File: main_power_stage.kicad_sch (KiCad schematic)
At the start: 75 parts, among them SW1 CAS-120TA, U11 AP7366_SOT, U2 LV14540DDAR, U6 TPS65987DDHRSHR, U7 LV14540DDAR, U8 74CBTLV3257_VQFN, U9 W25Q80DV_SOIC-8

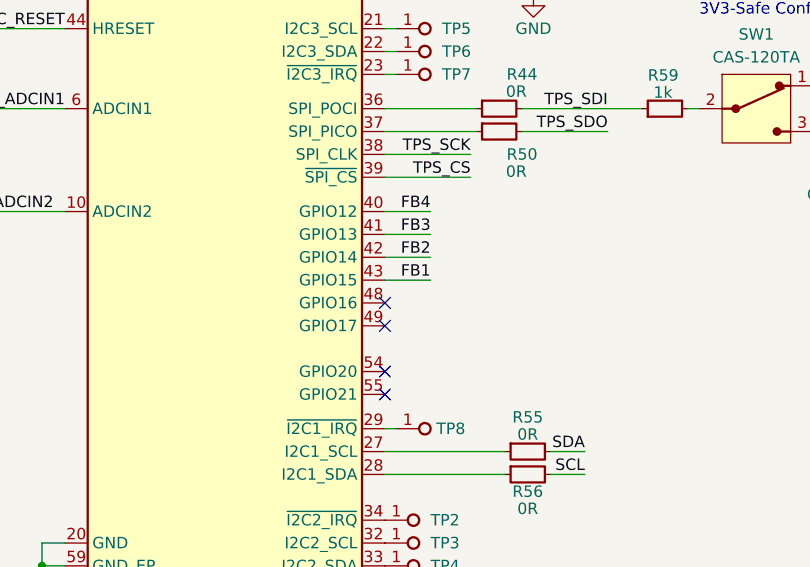
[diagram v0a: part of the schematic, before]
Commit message: [#63274] Change TPS65987 feedback for DCDC gpio pinout
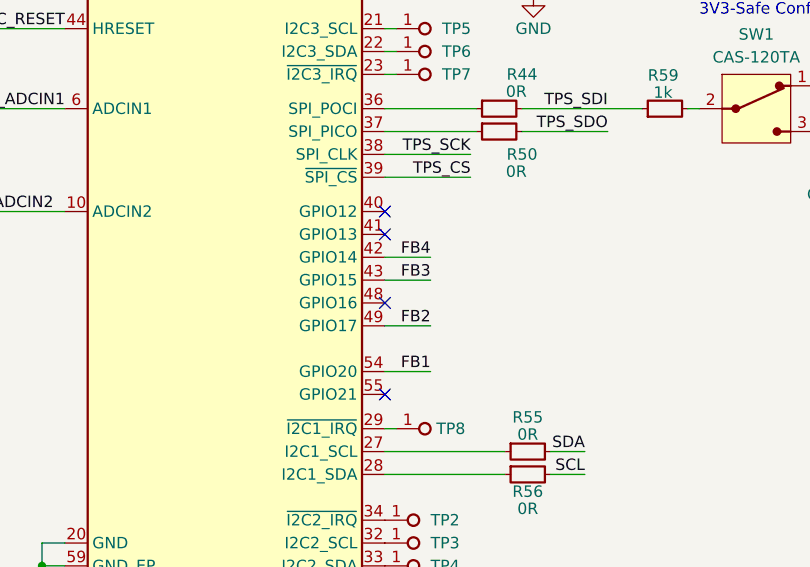
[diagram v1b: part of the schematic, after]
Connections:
- net FB1: now also U6.54 (GPIO20); no longer U6.43 (GPIO15)
- net FB2: now also U6.49 (GPIO17); no longer U6.42 (GPIO14)
- net FB3: now also U6.43 (GPIO15); no longer U6.41 (GPIO13)
- net FB4: now also U6.42 (GPIO14); no longer U6.40 (GPIO12)

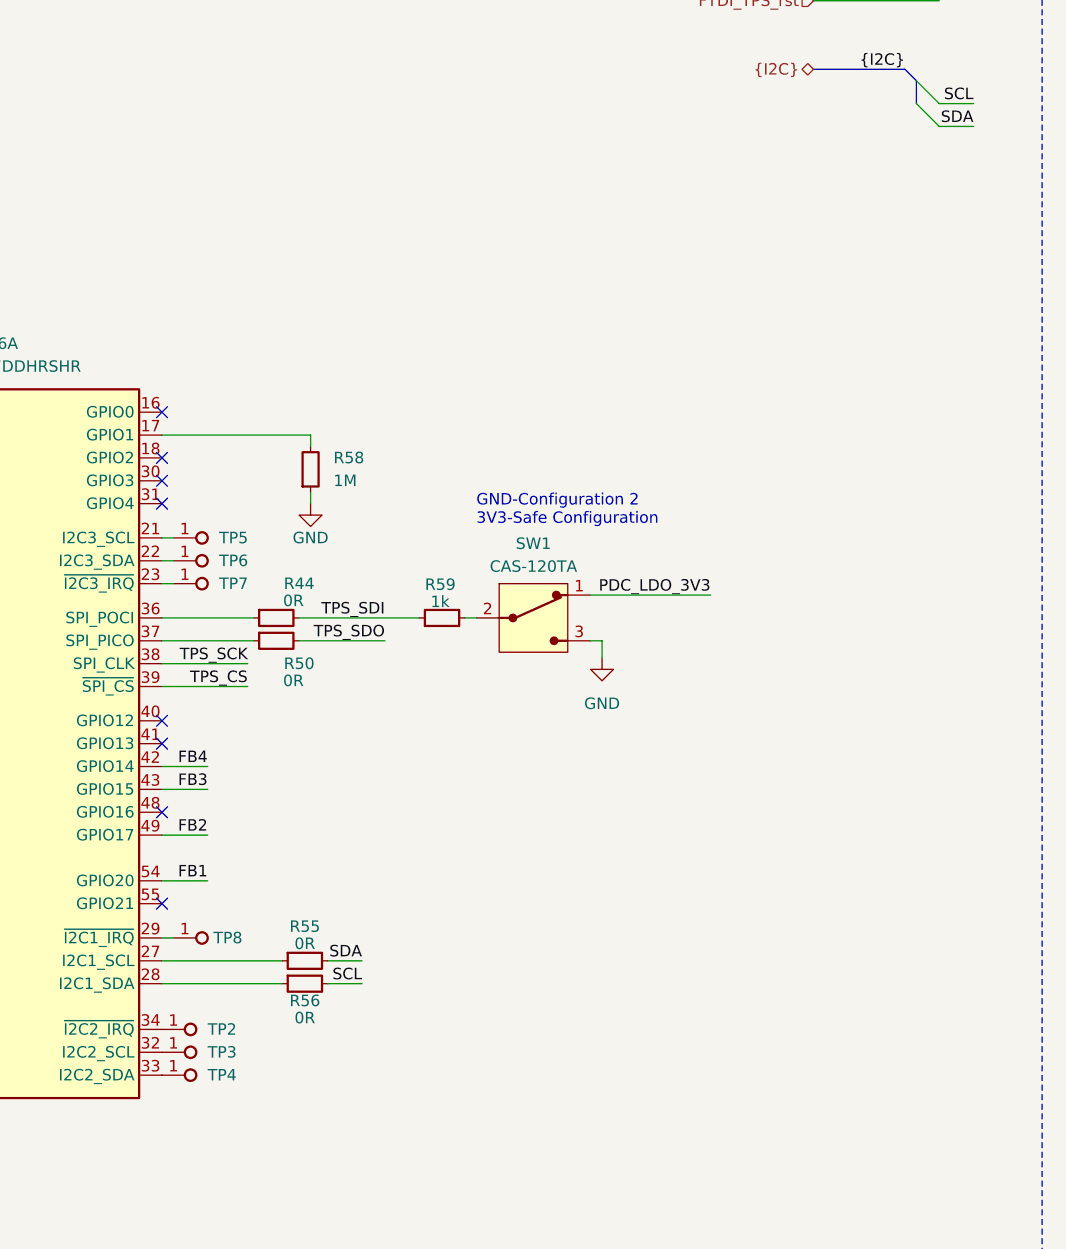
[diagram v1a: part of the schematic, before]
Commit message: [#63274] Add testpoints, improve silcscreen
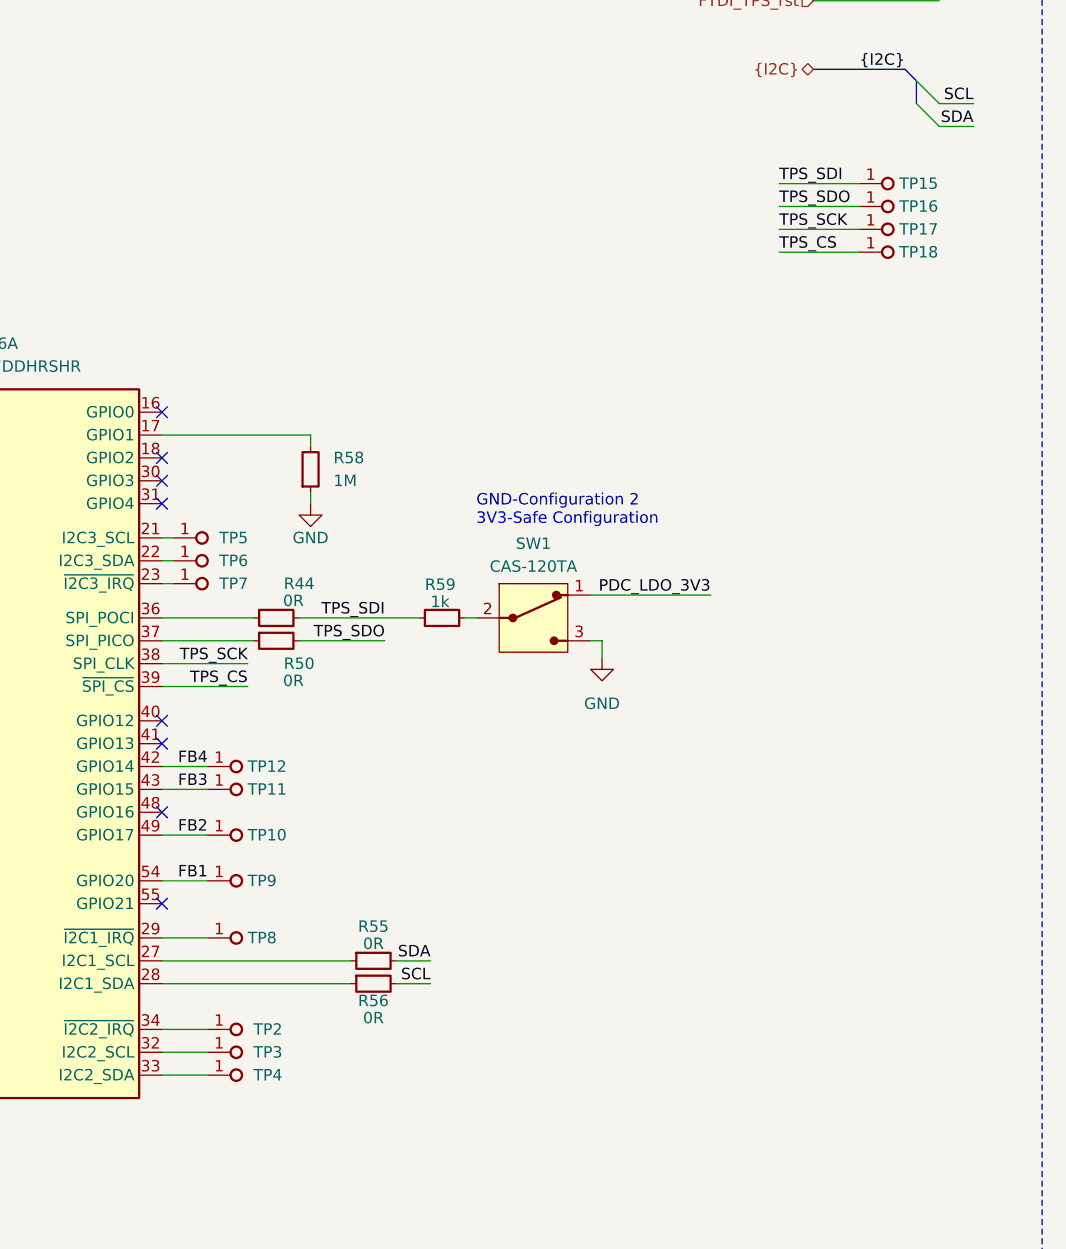
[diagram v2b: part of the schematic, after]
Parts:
- added TP10, TP11, TP12, TP15, TP16, TP17, TP18, TP9: TP_0.75mm_SMD, antmicro-footprints:TP_SMD_0.75mm, symbol antmicroTestPoints:TP_0.75mm_SMD
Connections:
- net FB1: now also TP9.1
- net FB2: now also TP10.1
- net FB3: now also TP11.1
- net FB4: now also TP12.1
- net TPS_CS: now also TP18.1
- net TPS_SCK: now also TP17.1
- net TPS_SDI: now also TP15.1
- net TPS_SDO: now also TP16.1
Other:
- moved on the sheet: R55, R56, TP2, TP3, TP4, TP8

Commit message: [#63274] Prepare for visualization and fabhouse
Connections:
- net FLASH_CS: now also TP18.1
- net FLASH_SCK: now also TP17.1
- net FLASH_SDI: now also TP16.1
- net FLASH_SDO: now also TP15.1
- net TPS_CS: no longer TP18.1
- net TPS_SCK: no longer TP17.1
- net TPS_SDI: no longer TP15.1
- net TPS_SDO: no longer TP16.1

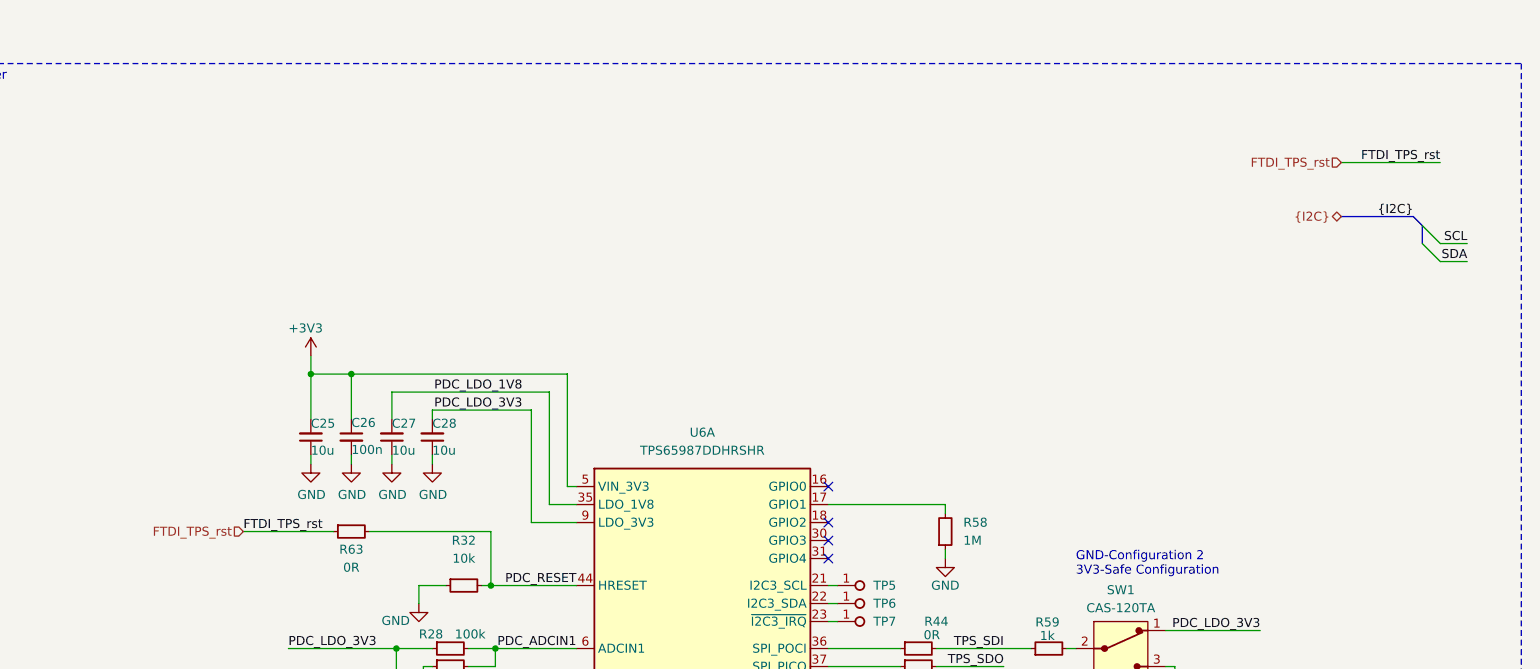
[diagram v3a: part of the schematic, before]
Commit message: [#63274] Add optocouplers for ETH diode, TPS65987D HRESET
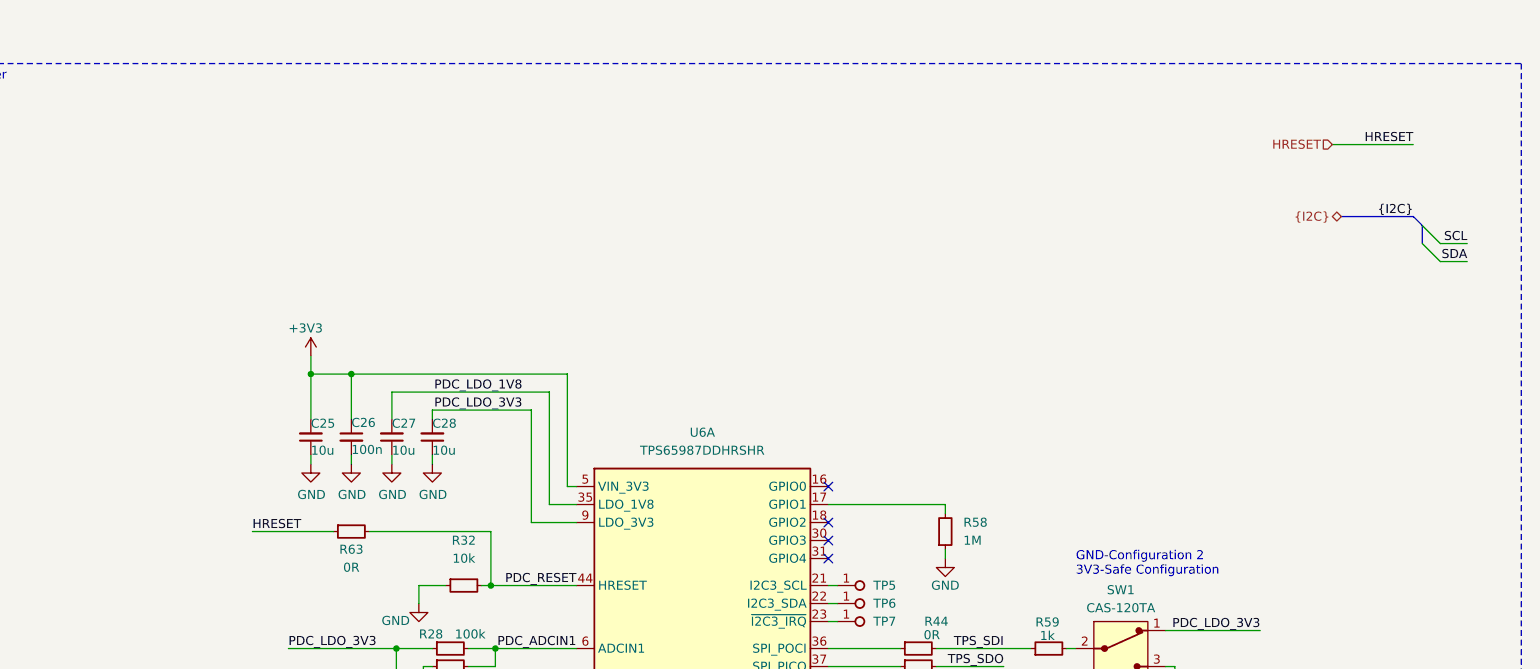
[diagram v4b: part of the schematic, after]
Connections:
- net FTDI_TPS_rst renamed HRESET
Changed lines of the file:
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@@
+    (stroke (width 0) (type default))
+  )
+  (wire (pts (xy 379.73 25.4) (xy 391.16 25.4))
     (stroke (width 0) (type default))
   )
@@
     (stroke (width 0) (type default))
   )
-  (wire (pts (xy 381 27.94) (xy 394.97 27.94))
-    (stroke (width 0) (type default))
-  )
   (wire (pts (xy 261.62 96.52) (xy 273.05 96.52))
     (stroke (width 0) (type default))
@@
     (stroke (width 0) (type default))
   )
-  (wire (pts (xy 226.06 80.01) (xy 238.76 80.01))
+  (wire (pts (xy 227.33 80.01) (xy 238.76 80.01))
     (stroke (width 0) (type default))
   )
@@
     (effects (font (size 1.27 1.27)) (justify right bottom))
   )
+  (label "HRESET" (at 391.16 25.4 180) (fields_autoplaced)
+    (effects (font (size 1.27 1.27)) (justify right bottom))
+  )
   (label "FB4" (at 162.56 97.79 180) (fields_autoplaced)
     (effects (font (size 1.27 1.27)) (justify right bottom))
@@
     (effects (font (size 1.27 1.27)) (justify left bottom))
   )
-  (label "FTDI_TPS_rst" (at 394.97 27.94 180) (fields_autoplaced)
-    (effects (font (size 1.27 1.27)) (justify right bottom))
-  )
   (label "SDA" (at 338.455 134.62 180) (fields_autoplaced)
     (effects (font (size 1.27 1.27)) (justify right bottom))
@@
     (effects (font (size 1.27 1.27)) (justify right bottom))
   )
-  (label "FTDI_TPS_rst" (at 226.06 80.01 0) (fields_autoplaced)
-    (effects (font (size 1.27 1.27)) (justify left bottom))
-  )
   (label "FTDI_SDO" (at 165.735 254 0) (fields_autoplaced)
     (effects (font (size 1.27 1.27)) (justify left bottom))
@@
     (effects (font (size 1.27 1.27)) (justify right bottom))
   )
+  (label "HRESET" (at 227.33 80.01 0) (fields_autoplaced)
+    (effects (font (size 1.27 1.27)) (justify left bottom))
+  )
   (label "FLASH_SCK" (at 222.885 254 0) (fields_autoplaced)
     (effects (font (size 1.27 1.27)) (justify left bottom))
@@
   (label "PDC_LDO_3V3" (at 222.885 251.46 0) (fields_autoplaced)
     (effects (font (size 1.27 1.27)) (justify left bottom))
-  )
-  (hierarchical_label "FTDI_TPS_rst" (shape input) (at 226.06 80.01 180) (fields_autoplaced)
-    (effects (font (size 1.27 1.27)) (justify right))
   )
   (hierarchical_label "{I2C}" (shape bidirectional) (at 381 35.56 180) (fields_autoplaced)
     (effects (font (size 1.27 1.27)) (justify right))
   )
+  (hierarchical_label "HRESET" (shape input) (at 379.73 25.4 180) (fields_autoplaced)
+    (effects (font (size 1.27 1.27)) (justify right))
+  )
   (hierarchical_label "{SPI}" (shape bidirectional) (at 269.24 198.12 180) (fields_autoplaced)
     (effects (font (size 1.27 1.27)) (justify right))
@@
     (effects (font (size 1.27 1.27)) (justify right))
   )
-  (hierarchical_label "FTDI_TPS_rst" (shape input) (at 381 27.94 180) (fields_autoplaced)
-    (effects (font (size 1.27 1.27)) (justify right))
-  )
